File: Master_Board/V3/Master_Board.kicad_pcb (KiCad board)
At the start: 2 copper layers, 137.4 x 98.3 mm, 200 parts, among them J101 649016227222, J201 Header_Male_Pin_2.54mm_1X3_,_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, J202 Header_Male_Pin_2.54mm_1X6_,_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, J301 Header_Male_Pin_2.54mm_1X2_,_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, J401 649006227222, J701 649004227222, J702 649004227222, J703 649004227222, J801 649002227222, J802 649002227222, J901 649002227222, J902 649002227222, J903 649002227222, J904 649002227222, Q1101 BSS806NH6327XTSA1, Q1102 BSS806NH6327XTSA1, Q1103 BSS806NH6327XTSA1, Q701 BC849BLT1G, Q702 BC849BLT1G, Q703 BC849BLT1G, Q704 BC849BLT1G, Q801 BC849BLT1G, Q802 BC849BLT1G, SW201 PTS645SM43SMTR92, SW202 PTS645SM43SMTR92, U201 STM32F446RE, U301 OKI-78SR-5/1.5-W36-C, U302 AZ1117IH-3.3TRG1, U401 SN65HVD232DR, U501 SN65HVD232DR, U901 ACPL-C87A-500E, U902 NCS1S2405SC, U903 ACPL-C87A-500E, U904 LMV321RILT, U905 LMV321RILT

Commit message: Rooting Master V3
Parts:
- added J704: 649002227222, Connectors:649002227222, F.Cu at (212.9, 45.0)
- added R712: RC0805JR-076K8L, Resistors:R0805, B.Cu at (219.2, 49.5)
- added U701: CPC1117NTR, IC:4-SOP, B.Cu at (217.9, 55.1)
- F102: value 39505000440 -> 39511000440
- moved J703 6.61 mm to (202.7, 45.0)
- moved F102 5.36 mm to (90.9, 58.9), turned to 90 degrees
- moved J702 4.57 mm to (190.0, 45.2)
- moved J701 1.91 mm to (177.7, 45.3)
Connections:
- F102 pad 2: 12V -> /Contactor_12V
- J901 pad 1: (no net) -> Net-(J901-Pad1)
- J902 pad 2: (no net) -> Net-(J902-Pad2)
- J903 pad 1: (no net) -> Net-(J903-Pad1)
- J904 pad 2: (no net) -> Net-(J904-Pad2)
- RL701 pad 1: (no net) -> Net-(RL701-Pad1)
- RL701 pad 4: (no net) -> Net-(RL701-Pad4)
- RL701 pad 7: 12V -> /ContactorControl/12V_Protected
- RL701 pad 8: 12V -> /ContactorControl/12V_Protected
- RL702 pad 1: (no net) -> Net-(RL702-Pad1)
- RL702 pad 4: (no net) -> Net-(RL702-Pad4)
- RL703 pad 1: (no net) -> Net-(RL703-Pad1)
- RL703 pad 4: (no net) -> Net-(RL703-Pad4)
- RL704 pad 1: (no net) -> Net-(RL704-Pad1)
- RL704 pad 4: (no net) -> Net-(RL704-Pad4)
- SW201 pad 1: (no net) -> Net-(SW201-Pad1)
- SW201 pad 3: (no net) -> Net-(SW201-Pad3)
- SW202 pad 2: (no net) -> Net-(SW202-Pad2)
- SW202 pad 4: (no net) -> Net-(SW202-Pad4)
- U201 pad 11: (no net) -> /PC3
- U201 pad 23: (no net) -> /PA7
- U201 pad 24: (no net) -> /PC4
- U201 pad 25: (no net) -> /PC5
- U201 pad 26: (no net) -> /PB0
- U201 pad 27: (no net) -> /PB1
- U201 pad 38: (no net) -> /PC7
- U201 pad 39: (no net) -> /PC8
- U201 pad 40: (no net) -> /PC9
- U201 pad 41: (no net) -> /PA8
- U201 pad 50: (no net) -> /PA15
- U201 pad 56: (no net) -> /PB4
- U201 pad 58: (no net) -> /PB6
- U201 pad 59: (no net) -> /PB7
- U201 pad 60: (no net) -> /BOOT0
- U201 pad 61: (no net) -> /PB8
- U201 pad 62: (no net) -> /PB9
- U401 pad 5: (no net) -> Net-(U401-Pad5)
- U401 pad 8: (no net) -> Net-(U401-Pad8)
- U501 pad 5: (no net) -> Net-(U501-Pad5)
- U501 pad 8: (no net) -> Net-(U501-Pad8)
- XTAL202 pad 2: (no net) -> Net-(XTAL202-Pad2)
- XTAL202 pad 3: (no net) -> Net-(XTAL202-Pad3)
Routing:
- net /Contactor_12V: track 0.00 -> 154.5 mm, vias 0 -> 1
- net /PC9: track 0.00 -> 118.5 mm, vias 0 -> 3
- net 12V: track 344.2 -> 231.8 mm, vias 5 -> 4
- net DGND: track 634.4 -> 713.2 mm
- net /ContactorControl/12V_Protected: track 0.00 -> 38.8 mm, vias 0 -> 2
- net 3.3V: track 211.6 -> 229.6 mm
- net /IO3: track 150.5 -> 135.1 mm
- net Net-(J701-Pad3): track 71.9 -> 57.8 mm
- net VDD: track 247.4 -> 241.5 mm, vias 10 -> 8
- net /IO2: track 233.9 -> 238.2 mm
- net Net-(D701-Pad2): track 4.10 -> 0.00 mm, vias 1 -> 0
- net Net-(R712-Pad1): track 0.00 -> 2.77 mm
- net /IO1: track 200.6 -> 202.4 mm, vias 1 -> 0
- net Net-(D1001-Pad1): track 3.45 -> 1.69 mm
- net /12V_IN2: track 18.7 -> 19.9 mm
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
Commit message: Silkscreen Master V3
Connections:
- D803 pad 1: 12V -> /Contactor_12V
- D804 pad 1: 12V -> /Contactor_12V
- J101 pad 12: 12V -> /IO4
- J101 pad 4: 12V -> /IO6
- R803 pad 1: 12V -> /Contactor_12V
- R804 pad 1: 12V -> /Contactor_12V
- RL801 pad 1: 12V -> /Contactor_12V
- RL802 pad 1: 12V -> /Contactor_12V
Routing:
- net /Contactor_12V: track 154.5 -> 268.3 mm, vias 1 -> 2
- net 12V: track 231.8 -> 152.2 mm
- net DGND: track 713.2 -> 687.9 mm, vias 25 -> 26
- net /IO3: track 135.1 -> 143.3 mm
- net CAN_PWR: track 151.5 -> 149.9 mm
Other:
- board text added: "(c) 2018 - Eclipse X"
- board text added: "BMS Master Board V3"
- board text added: "Pierre-Olivier Meilleur"
- board text removed: "(c) 2017 - Eclipse X"
- board text removed: "BMS Master Board V2"
- board text removed: "Julien G. Bourassa"

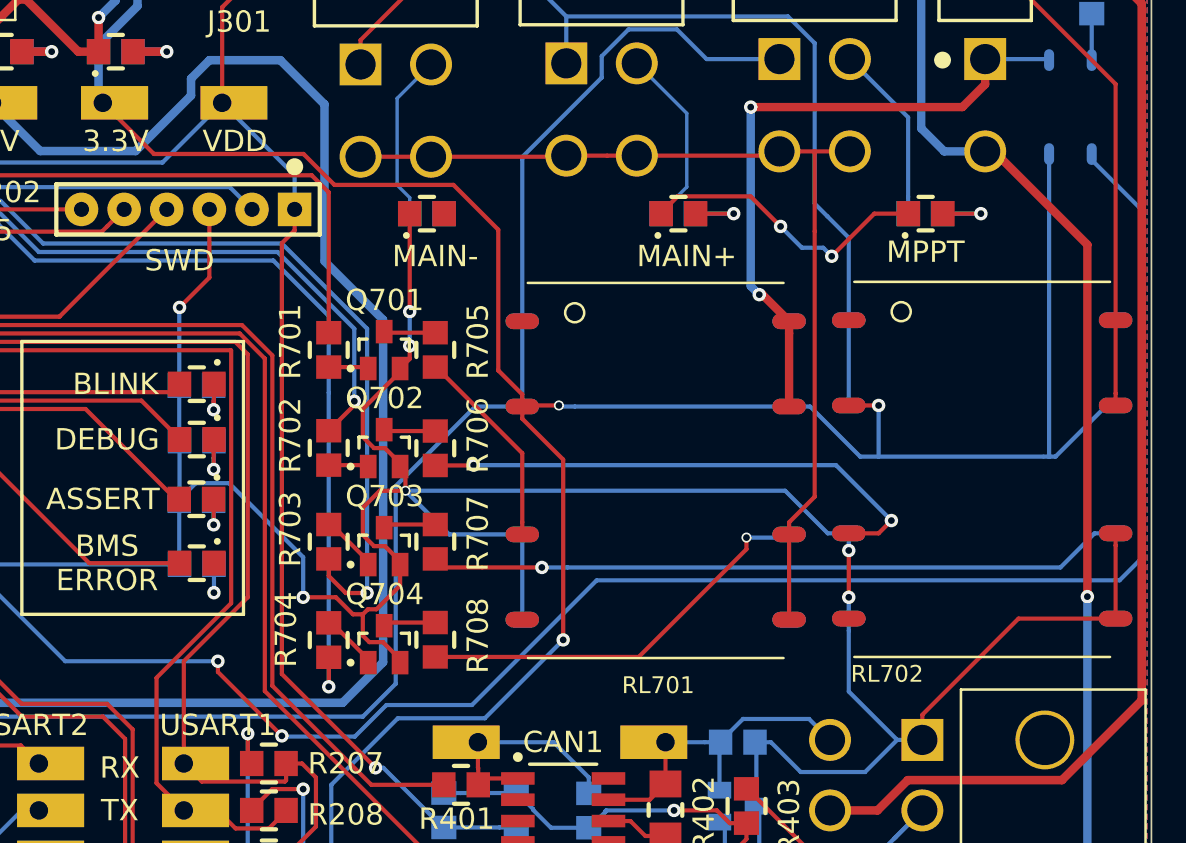
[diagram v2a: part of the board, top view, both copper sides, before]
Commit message: Correction of kill switch circuit
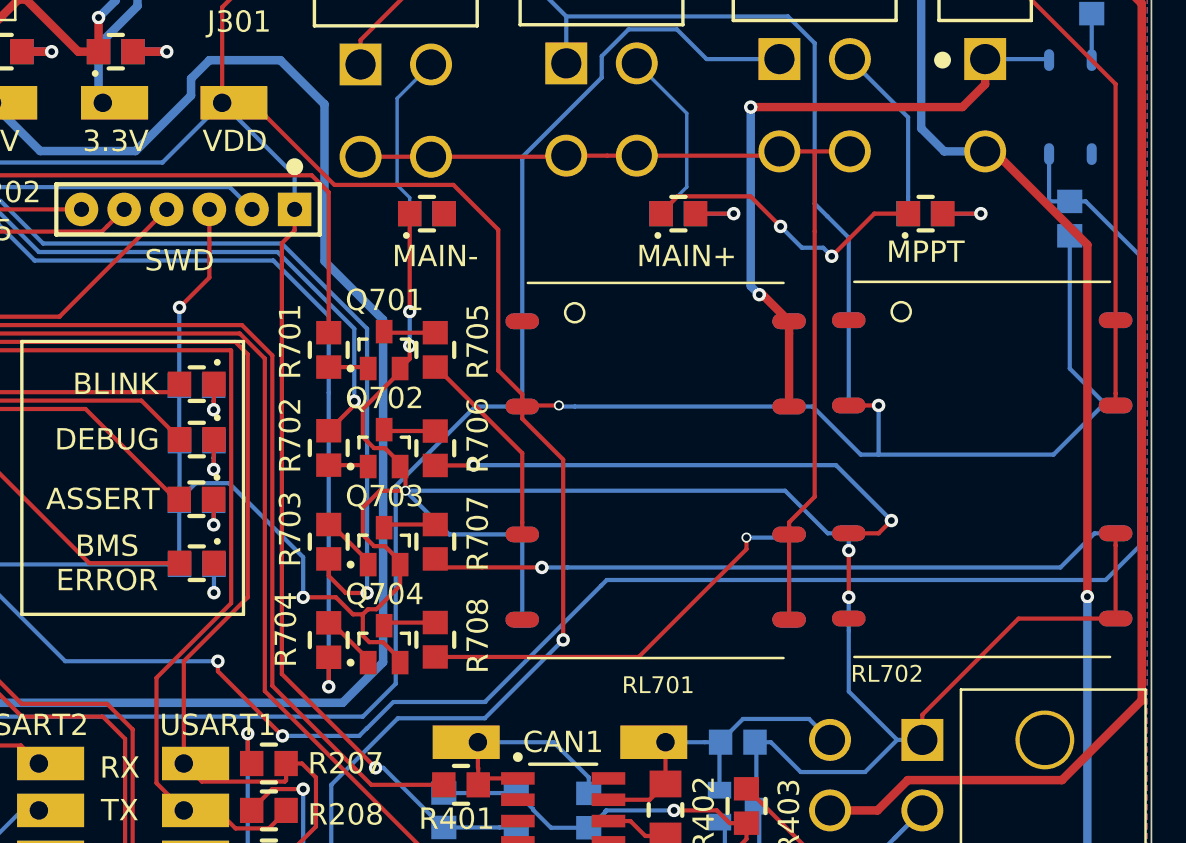
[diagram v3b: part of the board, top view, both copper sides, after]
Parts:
- added R713: RC0805JR-0710KL, Resistors:R0805, B.Cu at (217.9, 62.8)
- R712: value RC0805JR-076K8L -> RC0805JR-0747KL
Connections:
- RL701 pad 2: 3.3V -> VDD
- RL702 pad 2: 3.3V -> VDD
- RL703 pad 2: 3.3V -> VDD
- RL704 pad 2: 3.3V -> VDD
- U701 pad 3: /PC9 -> DGND
- U701 pad 4: 3.3V -> /PC9
- U904 pad 5: 3.3V -> VDD
- U905 pad 5: 3.3V -> VDD
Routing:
- net 3.3V: track 229.6 -> 33.0 mm, vias 3 -> 0
- net VDD: track 241.5 -> 423.8 mm, vias 8 -> 11
- net /PC9: track 118.8 -> 120.5 mm

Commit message: Changed values of optocoupler resistor
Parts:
- R705, R706, R707, R708: value RC0805JR-072K2L -> RC0805FR-071K1L
- R712: value RC0805JR-0747KL -> RC0805JR-0715KL
- moved G*** 4.58 mm to (120.1, 75.4)
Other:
- board text added: "Julien Bourassa/Pierre-Olivier Meilleur"
- board text removed: "Pierre-Olivier Meilleur"
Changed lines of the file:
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@@
-(kicad_pcb (version 4) (host pcbnew 4.0.6)
+(kicad_pcb (version 4) (host pcbnew 4.0.7)
   (general
     (links 381)
@@
       (effects (font (size 1.27 1.27) (thickness 0.254)))
     )
-    (fp_text value RC0805JR-072K2L (at 1.73 2.33 270) (layer F.Fab) hide
+    (fp_text value RC0805FR-071K1L (at 1.73 2.33 270) (layer F.Fab) hide
       (effects (font (size 1.27 1.27) (thickness 0.254)))
     )
@@
       (effects (font (size 1.27 1.27) (thickness 0.254)))
     )
-    (fp_text value RC0805JR-072K2L (at 1.73 2.33 270) (layer F.Fab) hide
+    (fp_text value RC0805FR-071K1L (at 1.73 2.33 270) (layer F.Fab) hide
       (effects (font (size 1.27 1.27) (thickness 0.254)))
     )
@@
       (effects (font (size 1.27 1.27) (thickness 0.254)))
     )
-    (fp_text value RC0805JR-072K2L (at 1.73 2.33 270) (layer F.Fab) hide
+    (fp_text value RC0805FR-071K1L (at 1.73 2.33 270) (layer F.Fab) hide
       (effects (font (size 1.27 1.27) (thickness 0.254)))
     )
@@
       (effects (font (size 1.27 1.27) (thickness 0.254)))
     )
-    (fp_text value RC0805JR-072K2L (at 1.73 2.33 270) (layer F.Fab) hide
+    (fp_text value RC0805FR-071K1L (at 1.73 2.33 270) (layer F.Fab) hide
       (effects (font (size 1.27 1.27) (thickness 0.254)))
     )
@@
   )
   (module Logo:Eclipse_logo_small (layer B.Cu)
-    (at 123.952 77.978 180)
+    (at 120.142 75.438 180)
     (fp_text reference G*** (at 0 0 180) (layer B.SilkS) hide
       (effects (font (thickness 0.3)) (justify mirror))
@@
       (effects (font (size 1.27 1.27) (thickness 0.254)) (justify mirror))
     )
-    (fp_text value RC0805JR-0747KL (at 1.73 -2.33 90) (layer B.Fab) hide
+    (fp_text value RC0805JR-0715KL (at 1.73 -2.33 90) (layer B.Fab) hide
       (effects (font (size 1.27 1.27) (thickness 0.254)) (justify mirror))
     )
@@
     (effects (font (size 1.27 1.27) (thickness 0.2032)))
   )
-  (gr_text "Pierre-Olivier Meilleur" (at 127.508 70.104) (layer B.SilkS)
+  (gr_text "Julien Bourassa/Pierre-Olivier Meilleur" (at 123.952 66.548) (layer B.SilkS)
     (effects (font (size 1.27 1.27) (thickness 0.2032)) (justify mirror))
   )
-  (gr_text "(c) 2018 - Eclipse X" (at 131.826 72.136) (layer B.SilkS)
+  (gr_text "(c) 2018 - Eclipse X" (at 129.032 69.088) (layer B.SilkS)
     (effects (font (size 1.27 1.27) (thickness 0.2032)) (justify mirror))
   )
-  (gr_text "BMS Master Board V3" (at 133.35 74.422) (layer B.SilkS)
+  (gr_text "BMS Master Board V3" (at 129.032 71.628) (layer B.SilkS)
     (effects (font (size 1.27 1.27) (thickness 0.2032)) (justify mirror))
   )
